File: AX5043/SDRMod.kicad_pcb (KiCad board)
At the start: 2 copper layers, 55.9 x 27.9 mm, 44 parts, among them P1 CONN_02X06, Q1 Q_NPN_BCE, Q2 RE1C002UNTCL, Q3 RE1C002UNTCL, Q4 RE1C002UNTCL, Q5 RE1C002UNTCL, Q6 RE1C002UNTCL, U1 AX5043, Y1 Crystal

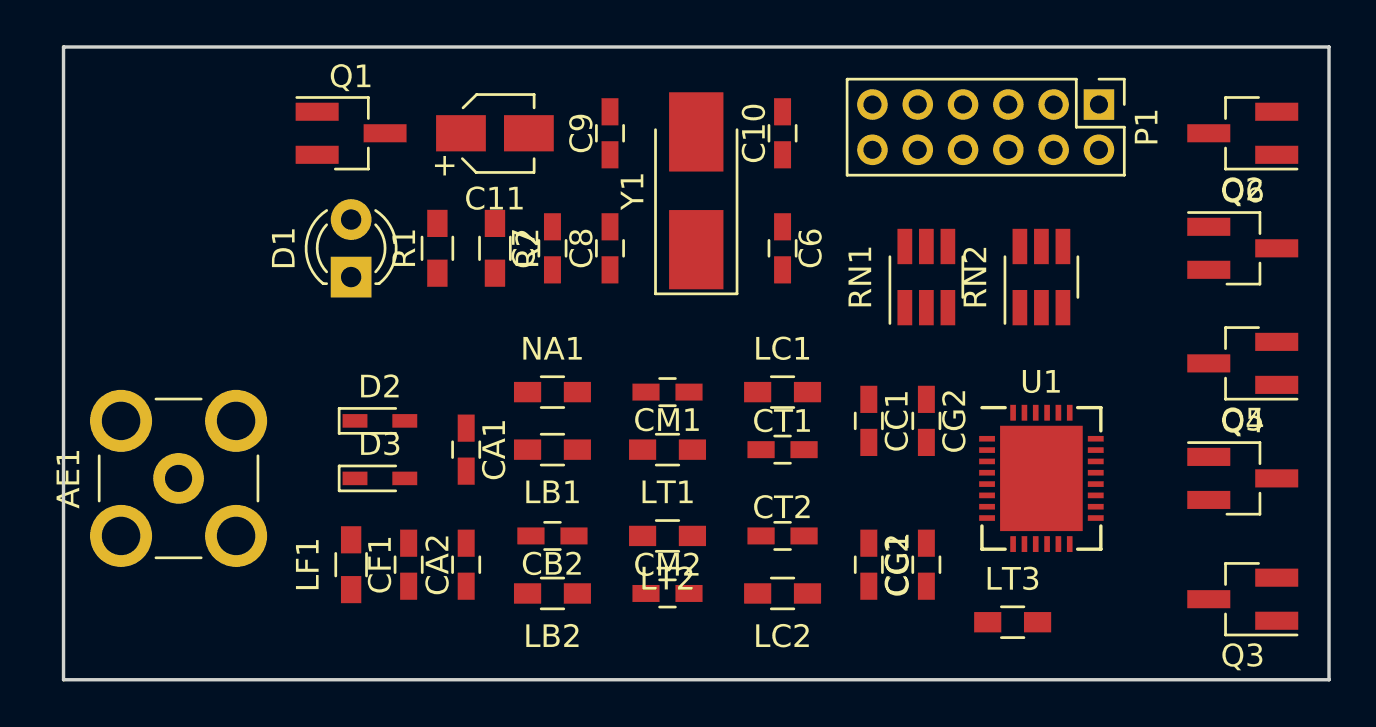
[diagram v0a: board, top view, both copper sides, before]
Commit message: AX5043 and level shifter splitted into two projects, IR removed
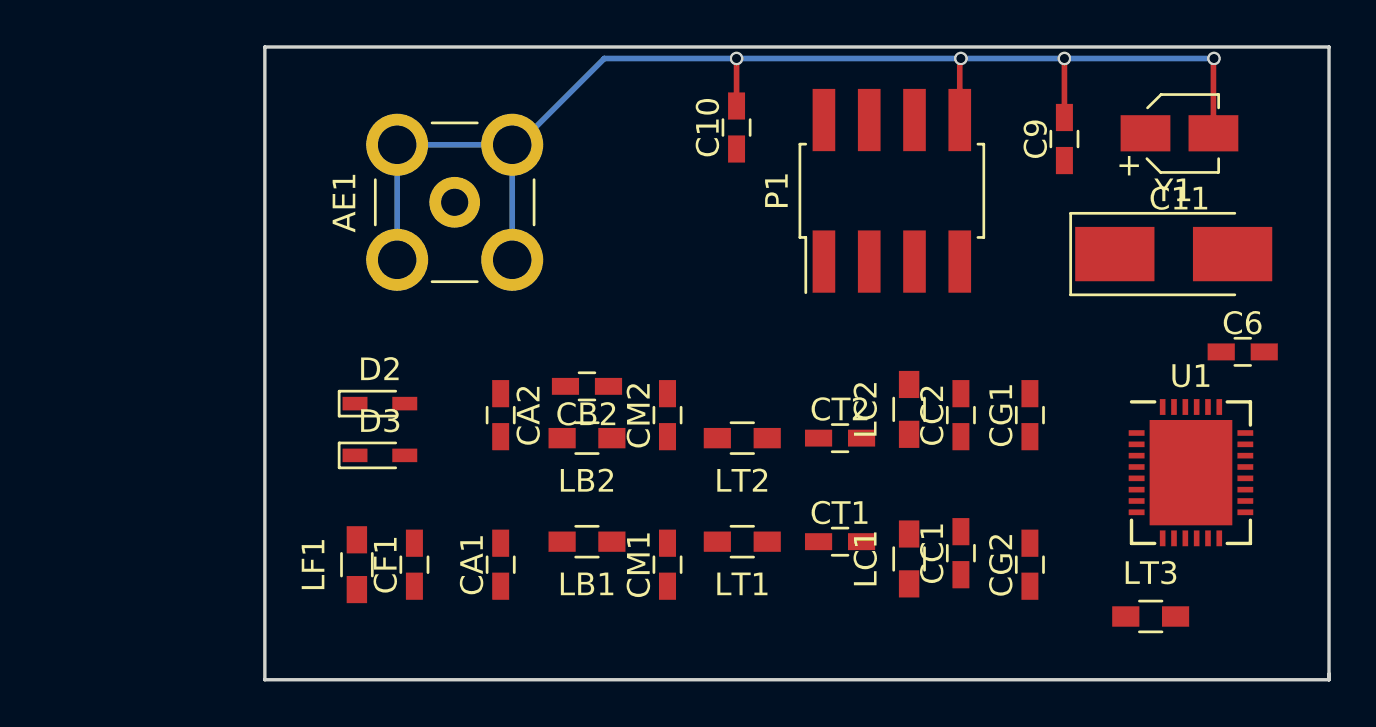
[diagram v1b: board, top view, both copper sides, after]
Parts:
- removed C7, C8: C, Capacitors_SMD:C_0603_HandSoldering
- removed D1: LED, LEDs:LED_D3.0mm
- removed NA1: L, Inductors_SMD:L_0603_HandSoldering
- removed Q1: Q_NPN_BCE, TO_SOT_Packages_SMD:SOT-23_Handsoldering
- removed Q2, Q3, Q4, Q5, Q6: RE1C002UNTCL, TO_SOT_Packages_SMD:SOT-23_Handsoldering
- removed R1, R2: R, Resistors_SMD:R_0603_HandSoldering
- removed RN1, RN2: R_Network05, TO_SOT_Packages_SMD:SOT-23-6_Handsoldering
- P1: value CONN_02X06 -> CONN_02X04; footprint Pin_Headers:Pin_Header_Straight_2x06_Pitch2.00mm -> Pin_Headers:Pin_Header_Straight_2x04_Pitch2.00mm_SMD
- moved C11 30.2 mm to (178.8, 108.0)
- moved Y1 21.3 mm to (178.6, 113.3), turned to 0 degrees
- moved C6 20.8 mm to (181.6, 117.6), turned to 0 degrees
- moved C9 20.1 mm to (173.7, 108.2)
- moved AE1 17.2 mm to (146.8, 111.0)
- moved P1 9.91 mm to (166.1, 110.5), turned to 90 degrees
- moved LC2 9.86 mm to (166.9, 120.1), turned to 90 degrees
- moved LC1 9.25 mm to (166.9, 126.7), turned to 90 degrees
- moved CG1 8.03 mm to (172.2, 120.4)
- moved CM2 7.87 mm to (156.2, 120.4), turned to 90 degrees
- moved CG2 7.82 mm to (172.2, 127.0), turned to 90 degrees
- moved CC2 7.75 mm to (169.2, 120.4), turned to 90 degrees
- moved CM1 7.62 mm to (156.2, 127.0), turned to 90 degrees
- moved CC1 7.12 mm to (169.2, 126.5), turned to 90 degrees
- moved LB2 7.03 mm to (152.7, 121.4)
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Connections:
- P1 pad 1: /MuC_Interrupt_IN -> +3V3
- P1 pad 2: +1V8 -> (no net)
- P1 pad 3: /MuC_SPI1_MISO -> Net-(P1-Pad3)
- P1 pad 4: +3V3 -> Net-(P1-Pad4)
- P1 pad 5: /MuC_SPI1_MOSI -> Net-(P1-Pad5)
- P1 pad 6: SYSCLK -> Net-(P1-Pad6)
- P1 pad 7: /MuC_SPI1_SCK -> Net-(P1-Pad7)
- P1 pad 8: DCLK -> GND
- U1 pad 11: DATA -> (no net)
- U1 pad 12: DCLK -> (no net)
- U1 pad 13: SYSCLK -> (no net)
- U1 pad 14: Net-(Q2-Pad1) -> Net-(P1-Pad4)
- U1 pad 15: Net-(Q6-Pad1) -> Net-(P1-Pad6)
- U1 pad 16: Net-(Q5-Pad1) -> Net-(P1-Pad7)
- U1 pad 17: Net-(Q4-Pad1) -> Net-(P1-Pad5)
- U1 pad 19: Net-(Q3-Pad1) -> Net-(P1-Pad3)
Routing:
- net GND: track 0.00 -> 58.6 mm, vias 0 -> 4
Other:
- board size 55.9 x 27.9 mm -> 47 x 27.9 mm
